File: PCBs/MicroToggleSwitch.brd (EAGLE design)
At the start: 10.5 x 31.7 mm, 3 parts

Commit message: Updated
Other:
- board size 10.5 x 31.7 mm -> 14.5 x 31.7 mm
- board text added: "PinwheelRobotics"
- board text added: "care@pinwheel.in"
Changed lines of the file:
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@@
 <setting verticaltext="up"/>
 </settings>
-<grid distance="50" unitdist="mil" unit="mm" style="lines" multiple="1" display="yes" altdistance="5" altunitdist="mil" altunit="mm"/>
+<grid distance="0.5" unitdist="mm" unit="mm" style="lines" multiple="1" display="yes" altdistance="5" altunitdist="mil" altunit="mm"/>
 <layers>
 <layer number="1" name="Top" color="4" fill="1" visible="yes" active="yes"/>
@@
 <layer number="43" name="vRestrict" color="2" fill="10" visible="yes" active="yes"/>
 <layer number="44" name="Drills" color="7" fill="1" visible="no" active="yes"/>
-<layer number="45" name="Holes" color="7" fill="1" visible="no" active="yes"/>
+<layer number="45" name="Holes" color="7" fill="1" visible="yes" active="yes"/>
 <layer number="46" name="Milling" color="3" fill="1" visible="no" active="yes"/>
 <layer number="47" name="Measures" color="7" fill="1" visible="no" active="yes"/>
@@
 <board>
 <plain>
-<wire x1="15.1" y1="11.43" x2="25.578" y2="11.43" width="0" layer="20"/>
-<wire x1="25.578" y1="11.43" x2="25.578" y2="43.17" width="0" layer="20"/>
-<wire x1="25.578" y1="43.17" x2="15.1" y2="43.17" width="0" layer="20"/>
-<wire x1="15.1" y1="43.17" x2="15.1" y2="11.43" width="0" layer="20"/>
+<wire x1="13" y1="41.531628125" x2="13" y2="13.06995625" width="0" layer="20"/>
+<wire x1="13" y1="13.06995625" x2="14.63995625" y2="11.43" width="0" layer="20" curve="90"/>
+<wire x1="14.63995625" y1="11.43" x2="25.88049375" y2="11.43" width="0" layer="20"/>
+<wire x1="25.88049375" y1="11.43" x2="27.5" y2="13.04950625" width="0" layer="20" curve="90"/>
+<wire x1="27.5" y1="13.04950625" x2="27.5" y2="41.55424375" width="0" layer="20"/>
+<wire x1="27.5" y1="41.55424375" x2="25.88424375" y2="43.17" width="0" layer="20" curve="90"/>
+<wire x1="25.88424375" y1="43.17" x2="14.638371875" y2="43.17" width="0" layer="20"/>
+<wire x1="14.638371875" y1="43.17" x2="13" y2="41.531628125" width="0" layer="20" curve="90"/>
+<hole x="14.986" y="41.021" drill="3"/>
+<hole x="25.4" y="41.021" drill="3"/>
+<hole x="15" y="13.5" drill="3"/>
+<hole x="25.527" y="13.486" drill="3"/>
+<text x="15.621" y="18.415" size="1.778" layer="21" rot="R90">PinwheelRobotics </text>
+<text x="27.051" y="36.957" size="1.778" layer="22" rot="MR270">care@pinwheel.in</text>
 </plain>
 <attributes>
@@
 </element>
 <element name="U$1" library="microbit" package="MICROBIT_PAD" value="MICROBIT_PAD" x="20.32" y="18.542" smashed="yes">
-<attribute name="NAME" x="25.146" y="12.7" size="1.27" layer="21" rot="R90"/>
+<attribute name="NAME" x="25.019" y="16.637" size="1.27" layer="21" rot="R90"/>
 </element>
 <element name="U$2" library="microbit" package="MICROBIT_PAD" value="MICROBIT_PAD" x="20.32" y="36.068" smashed="yes" rot="R180">

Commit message: New Update
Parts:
- moved U$1 0.13 mm to (20.3, 18.4)
- moved U$2 0.13 mm to (20.3, 35.9)
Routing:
- net N$2: track 14.4 -> 7.77 mm
- net N$1: track 14.4 -> 8.05 mm
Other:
- board size 14.5 x 31.7 mm -> 14.5 x 31.6 mm
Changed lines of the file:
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@@
 <drawing>
 <settings>
-<setting alwaysvectorfont="yes"/>
+<setting alwaysvectorfont="no"/>
 <setting verticaltext="up"/>
 </settings>
@@
 <wire x1="25.88049375" y1="11.43" x2="27.5" y2="13.04950625" width="0" layer="20" curve="90"/>
 <wire x1="27.5" y1="13.04950625" x2="27.5" y2="41.55424375" width="0" layer="20"/>
-<wire x1="27.5" y1="41.55424375" x2="25.88424375" y2="43.17" width="0" layer="20" curve="90"/>
-<wire x1="25.88424375" y1="43.17" x2="14.638371875" y2="43.17" width="0" layer="20"/>
-<wire x1="14.638371875" y1="43.17" x2="13" y2="41.531628125" width="0" layer="20" curve="90"/>
-<hole x="14.986" y="41.021" drill="3"/>
-<hole x="25.4" y="41.021" drill="3"/>
+<wire x1="27.5" y1="41.55424375" x2="25.88424375" y2="43" width="0" layer="20" curve="90"/>
+<wire x1="25.88424375" y1="43" x2="14.638371875" y2="43" width="0" layer="20"/>
+<wire x1="14.638371875" y1="43" x2="13" y2="41.531628125" width="0" layer="20" curve="90"/>
+<hole x="15" y="41" drill="3"/>
+<hole x="25.5" y="41" drill="3"/>
 <hole x="15" y="13.5" drill="3"/>
-<hole x="25.527" y="13.486" drill="3"/>
+<hole x="25.5" y="13.5" drill="3"/>
 <text x="15.621" y="18.415" size="1.778" layer="21" rot="R90">PinwheelRobotics </text>
 <text x="27.051" y="36.957" size="1.778" layer="22" rot="MR270">care@pinwheel.in</text>
@@
 <attribute name="SF_SKU" value="COM-00097" x="-1.27" y="62.865" size="1.778" layer="27" rot="R180" display="off"/>
 </element>
-<element name="U$1" library="microbit" package="MICROBIT_PAD" value="MICROBIT_PAD" x="20.32" y="18.542" smashed="yes">
-<attribute name="NAME" x="25.019" y="16.637" size="1.27" layer="21" rot="R90"/>
+<element name="U$1" library="microbit" package="MICROBIT_PAD" value="MICROBIT_PAD" x="20.32" y="18.415" smashed="yes">
+<attribute name="NAME" x="25.019" y="16.51" size="1.27" layer="21" rot="R90"/>
 </element>
-<element name="U$2" library="microbit" package="MICROBIT_PAD" value="MICROBIT_PAD" x="20.32" y="36.068" smashed="yes" rot="R180">
-<attribute name="NAME" x="24.384" y="38.227" size="1.27" layer="21" rot="R270"/>
+<element name="U$2" library="microbit" package="MICROBIT_PAD" value="MICROBIT_PAD" x="20.32" y="35.941" smashed="yes" rot="R180">
+<attribute name="NAME" x="24.384" y="38.1" size="1.27" layer="21" rot="R270"/>
 </element>
 </elements>
@@
 <contactref element="U$1" pad="PAD"/>
 <contactref element="S1" pad="1"/>
-<wire x1="23.3172" y1="15.3924" x2="23.622" y2="15.6972" width="0.1524" layer="16"/>
-<wire x1="20.4216" y1="15.3924" x2="23.3172" y2="15.3924" width="0.1524" layer="16"/>
-<wire x1="20.32" y1="18.542" x2="20.4216" y2="15.3924" width="0.1524" layer="16"/>
 <wire x1="23.622" y1="24.9936" x2="23.5712" y2="25.0444" width="0.1524" layer="16"/>
-<wire x1="23.5712" y1="25.0444" x2="23.5712" y2="21.7932" width="1.27" layer="16"/>
-<wire x1="23.5712" y1="21.7932" x2="20.32" y2="18.542" width="1.27" layer="16"/>
+<wire x1="23.5712" y1="25.0444" x2="23.5712" y2="21.6662" width="1.27" layer="16"/>
+<wire x1="23.5712" y1="21.6662" x2="20.32" y2="18.415" width="1.27" layer="16"/>
 </signal>
 <signal name="N$2">
 <contactref element="U$2" pad="PAD"/>
 <contactref element="S1" pad="3"/>
-<wire x1="23.622" y1="39.1668" x2="23.7744" y2="39.0144" width="0.1524" layer="16"/>
-<wire x1="20.574" y1="39.1668" x2="23.622" y2="39.1668" width="0.1524" layer="16"/>
-<wire x1="20.2692" y1="38.862" x2="20.574" y2="39.1668" width="0.1524" layer="16"/>
 <wire x1="23.622" y1="29.5656" x2="23.5712" y2="29.5656" width="0.1524" layer="16"/>
-<wire x1="20.2692" y1="38.862" x2="20.32" y2="36.068" width="0.1524" layer="16"/>
 <wire x1="23.5712" y1="29.5656" x2="20.32" y2="32.8168" width="1.27" layer="16"/>
-<wire x1="20.32" y1="32.8168" x2="20.32" y2="36.068" width="1.27" layer="16"/>
+<wire x1="20.32" y1="32.8168" x2="20.32" y2="35.941" width="1.27" layer="16"/>
 </signal>
 </signals>

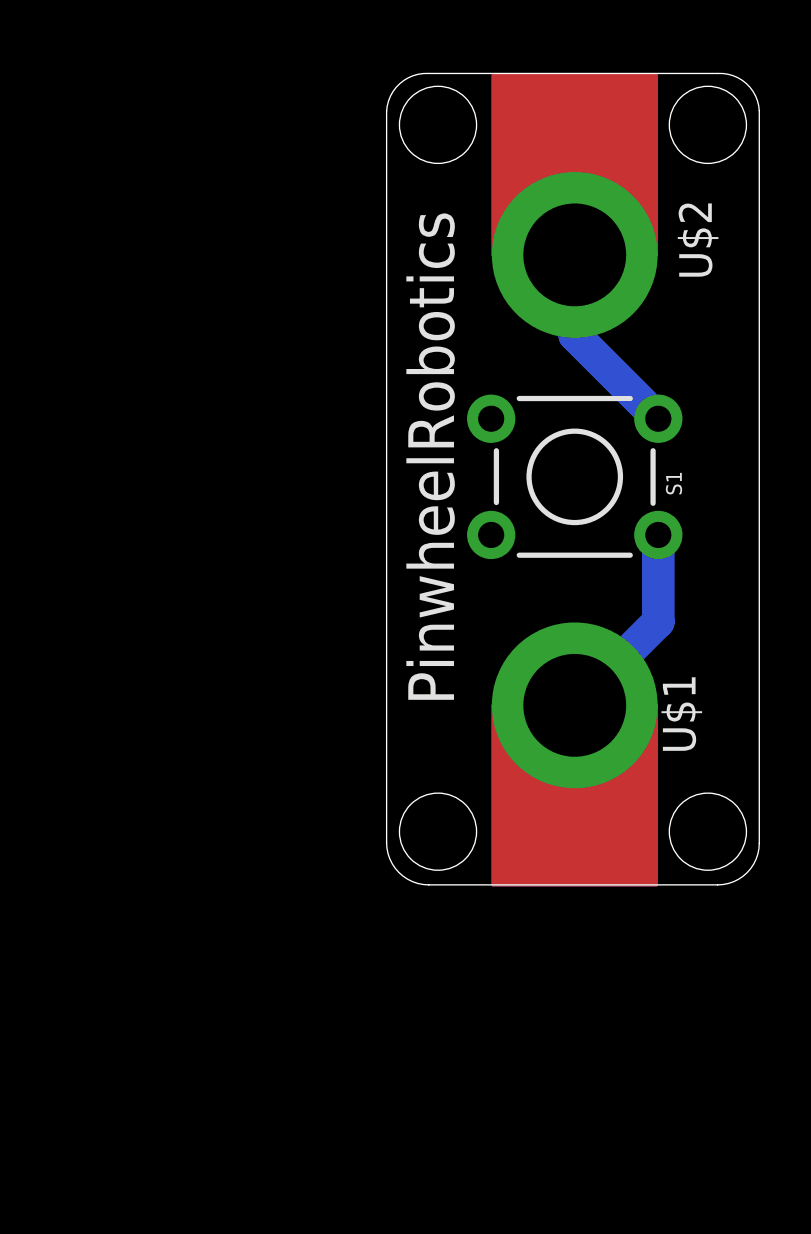
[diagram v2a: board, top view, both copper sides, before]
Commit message: New Update for board curv
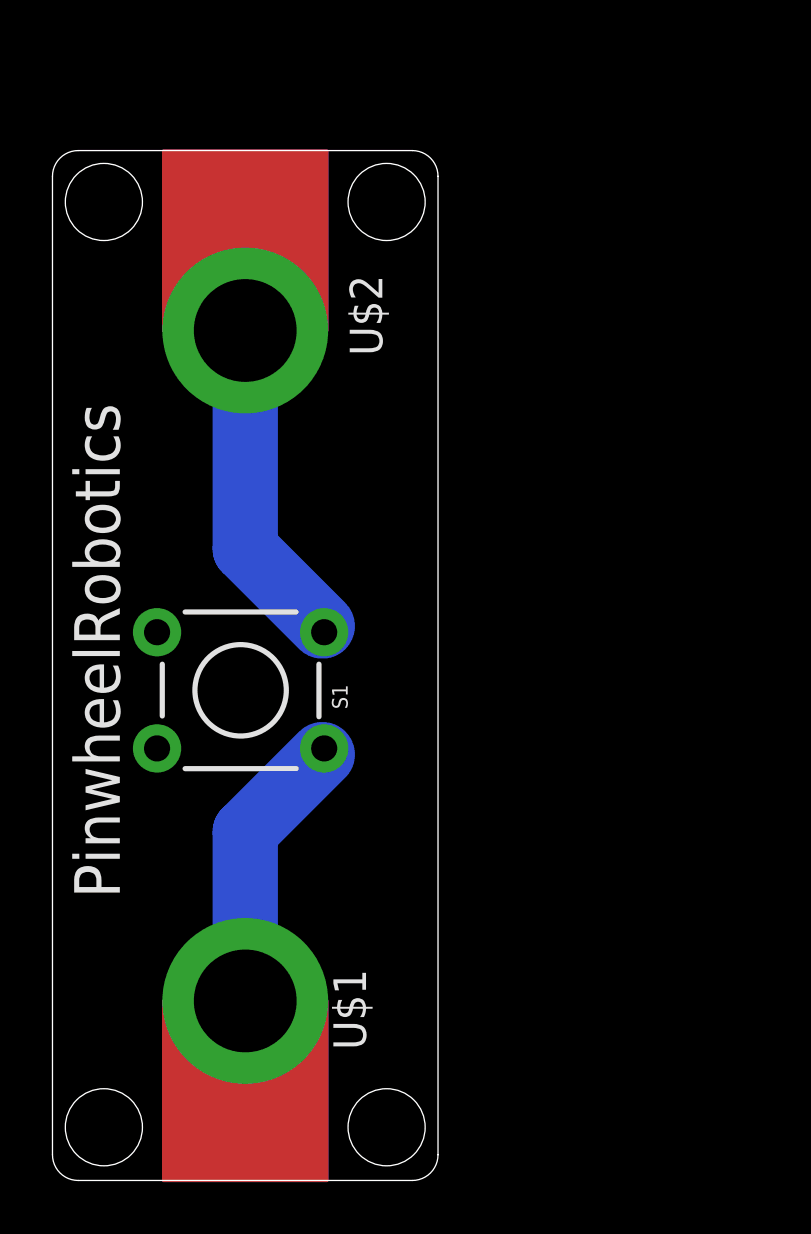
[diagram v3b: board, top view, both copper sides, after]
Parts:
- moved U$1 17.2 mm to (7.50, 6.92)
- moved S1 15.4 mm to (7.32, 19.0)
- moved U$2 13.2 mm to (7.50, 33.0)
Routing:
- net N$2: track 7.77 -> 13.0 mm
- net N$1: track 8.05 -> 11.1 mm
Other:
- board size 14.5 x 31.6 mm -> 15 x 40.1 mm
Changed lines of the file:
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@@
 <drawing>
 <settings>
-<setting alwaysvectorfont="no"/>
+<setting alwaysvectorfont="yes"/>
 <setting verticaltext="up"/>
 </settings>
@@
 <board>
 <plain>
-<wire x1="13" y1="41.531628125" x2="13" y2="13.06995625" width="0" layer="20"/>
-<wire x1="13" y1="13.06995625" x2="14.63995625" y2="11.43" width="0" layer="20" curve="90"/>
-<wire x1="14.63995625" y1="11.43" x2="25.88049375" y2="11.43" width="0" layer="20"/>
-<wire x1="25.88049375" y1="11.43" x2="27.5" y2="13.04950625" width="0" layer="20" curve="90"/>
-<wire x1="27.5" y1="13.04950625" x2="27.5" y2="41.55424375" width="0" layer="20"/>
-<wire x1="27.5" y1="41.55424375" x2="25.88424375" y2="43" width="0" layer="20" curve="90"/>
-<wire x1="25.88424375" y1="43" x2="14.638371875" y2="43" width="0" layer="20"/>
-<wire x1="14.638371875" y1="43" x2="13" y2="41.531628125" width="0" layer="20" curve="90"/>
-<hole x="15" y="41" drill="3"/>
-<hole x="25.5" y="41" drill="3"/>
-<hole x="15" y="13.5" drill="3"/>
-<hole x="25.5" y="13.5" drill="3"/>
-<text x="15.621" y="18.415" size="1.778" layer="21" rot="R90">PinwheelRobotics </text>
-<text x="27.051" y="36.957" size="1.778" layer="22" rot="MR270">care@pinwheel.in</text>
+<wire x1="0" y1="39" x2="0" y2="0.93" width="0" layer="20"/>
+<wire x1="0" y1="0.93" x2="1" y2="-0.07" width="0" layer="20" curve="90"/>
+<wire x1="1" y1="-0.07" x2="14" y2="-0.07" width="0" layer="20"/>
+<wire x1="14" y1="-0.07" x2="15" y2="0.93" width="0" layer="20" curve="90"/>
+<wire x1="15" y1="0.93" x2="15" y2="39" width="0" layer="20"/>
+<wire x1="15" y1="39" x2="14" y2="40" width="0" layer="20" curve="90"/>
+<wire x1="14" y1="40" x2="1" y2="40" width="0" layer="20"/>
+<wire x1="1" y1="40" x2="0" y2="39" width="0" layer="20" curve="90"/>
+<hole x="2" y="38" drill="3"/>
+<hole x="13" y="38" drill="3"/>
+<hole x="2" y="2" drill="3"/>
+<hole x="13" y="2" drill="3"/>
+<text x="2.621" y="10.915" size="1.778" layer="21" rot="R90">PinwheelRobotics </text>
+<text x="14.051" y="30.457" size="1.778" layer="22" rot="MR270">care@pinwheel.in</text>
 </plain>
 <attributes>
@@
 </autorouter>
 <elements>
-<element name="S1" library="SparkFun-Switches" library_urn="urn:adsk.eagle:library:535" package="TACTILE_SWITCH_PTH_6.0MM" package3d_urn="urn:adsk.eagle:package:40163/1" value="MOMENTARY-SWITCH-SPST-PTH-6.0MM" x="20.32" y="27.305" smashed="yes" rot="R180">
-<attribute name="NAME" x="23.876" y="27.051" size="0.6096" layer="25" font="vector" ratio="20" rot="R270" align="bottom-center"/>
-<attribute name="PROD_ID" value=" SWCH-08441" x="-1.27" y="62.865" size="1.778" layer="27" rot="R180" display="off"/>
-<attribute name="SF_SKU" value="COM-00097" x="-1.27" y="62.865" size="1.778" layer="27" rot="R180" display="off"/>
+<element name="S1" library="SparkFun-Switches" library_urn="urn:adsk.eagle:library:535" package="TACTILE_SWITCH_PTH_6.0MM" package3d_urn="urn:adsk.eagle:package:40163/1" value="MOMENTARY-SWITCH-SPST-PTH-6.0MM" x="7.32" y="19" smashed="yes" rot="R180">
+<attribute name="NAME" x="10.876" y="18.746" size="0.6096" layer="25" font="vector" ratio="20" rot="R270" align="bottom-center"/>
+<attribute name="PROD_ID" value=" SWCH-08441" x="-14.27" y="54.56" size="1.778" layer="27" rot="R180" display="off"/>
+<attribute name="SF_SKU" value="COM-00097" x="-14.27" y="54.56" size="1.778" layer="27" rot="R180" display="off"/>
 </element>
-<element name="U$1" library="microbit" package="MICROBIT_PAD" value="MICROBIT_PAD" x="20.32" y="18.415" smashed="yes">
-<attribute name="NAME" x="25.019" y="16.51" size="1.27" layer="21" rot="R90"/>
+<element name="U$1" library="microbit" package="MICROBIT_PAD" value="MICROBIT_PAD" x="7.5" y="6.915" smashed="yes">
+<attribute name="NAME" x="12.199" y="5.01" size="1.27" layer="21" rot="R90"/>
 </element>
-<element name="U$2" library="microbit" package="MICROBIT_PAD" value="MICROBIT_PAD" x="20.32" y="35.941" smashed="yes" rot="R180">
-<attribute name="NAME" x="24.384" y="38.1" size="1.27" layer="21" rot="R270"/>
+<element name="U$2" library="microbit" package="MICROBIT_PAD" value="MICROBIT_PAD" x="7.5" y="33" smashed="yes" rot="R180">
+<attribute name="NAME" x="11.564" y="35.159" size="1.27" layer="21" rot="R270"/>
 </element>
 </elements>
@@
 <contactref element="U$1" pad="PAD"/>
 <contactref element="S1" pad="1"/>
-<wire x1="23.622" y1="24.9936" x2="23.5712" y2="25.0444" width="0.1524" layer="16"/>
-<wire x1="23.5712" y1="25.0444" x2="23.5712" y2="21.6662" width="1.27" layer="16"/>
-<wire x1="23.5712" y1="21.6662" x2="20.32" y2="18.415" width="1.27" layer="16"/>
+<wire x1="7.5" y1="13.5" x2="10.5" y2="16.5" width="2.54" layer="16"/>
+<wire x1="7.5" y1="6.915" x2="7.5" y2="13.5" width="2.54" layer="16"/>
+<wire x1="10.5" y1="16.5" x2="10.5712" y2="16.7394" width="0.1524" layer="16"/>
 </signal>
 <signal name="N$2">
 <contactref element="U$2" pad="PAD"/>
 <contactref element="S1" pad="3"/>
-<wire x1="23.622" y1="29.5656" x2="23.5712" y2="29.5656" width="0.1524" layer="16"/>
-<wire x1="23.5712" y1="29.5656" x2="20.32" y2="32.8168" width="1.27" layer="16"/>
-<wire x1="20.32" y1="32.8168" x2="20.32" y2="35.941" width="1.27" layer="16"/>
+<wire x1="7.5" y1="24.5" x2="10.5" y2="21.5" width="2.54" layer="16"/>
+<wire x1="7.5" y1="33" x2="7.5" y2="24.5" width="2.54" layer="16"/>
+<wire x1="10.5" y1="21.5" x2="10.5712" y2="21.2606" width="0.1524" layer="16"/>
 </signal>
 </signals>
